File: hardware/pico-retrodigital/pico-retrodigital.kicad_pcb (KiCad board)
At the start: 2 copper layers, 50 x 38 mm, 70 parts, among them J1 Conn_02x05_Top_Bottom, J3 Conn_01x14, J4 Conn_01x02_Pin, J5 USB_C_Plug_USB2.0, U1 SN74LVC1G17DBVR, U2 SN74LVC1G17DBVR, U3 RP2354B, U4 SN74LVC245APW, U5 SN74LVC245APW, U6 SN74LVC245APW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

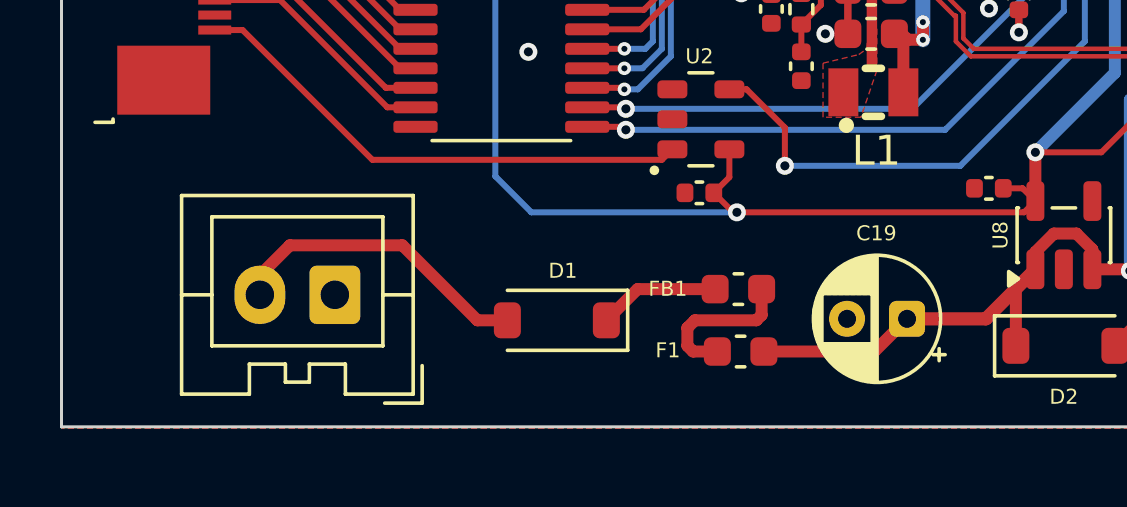
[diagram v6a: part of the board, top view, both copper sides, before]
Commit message: Add JLCPCB part numbers
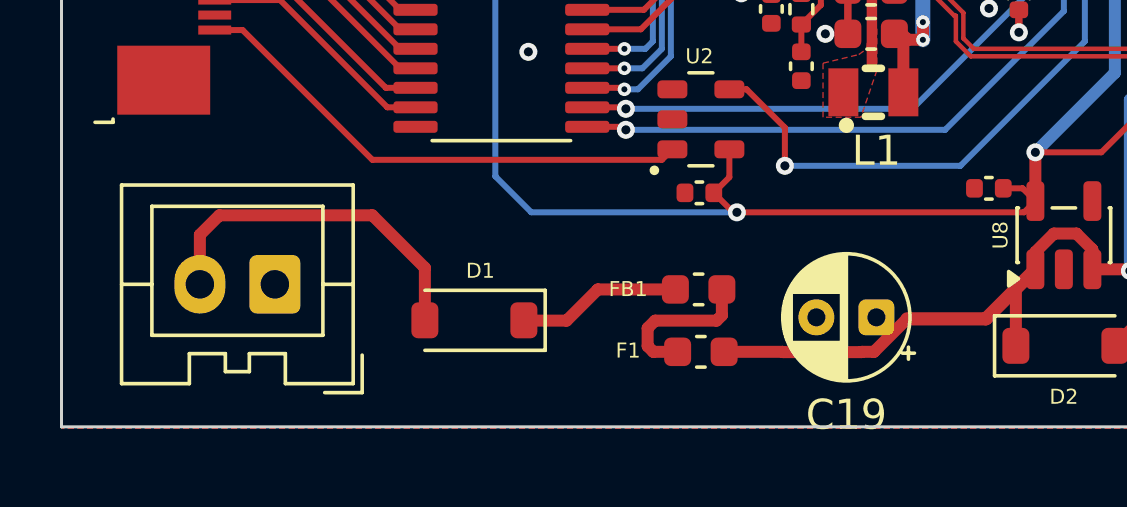
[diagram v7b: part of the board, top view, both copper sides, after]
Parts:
- moved D1 2.75 mm to (56.2, 109.9)
- moved J4 2.03 mm to (49.5, 108.7)
- moved F1 1.33 mm to (63.8, 111.0)
- moved FB1 1.33 mm to (63.7, 108.9)
- moved C19 1.02 mm to (69.6, 109.8)
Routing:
- net +5V MVS: track 10.3 -> 11.9 mm
- net Net-(D1-K): track 4.06 -> 5.48 mm
- net +5V: track 34.9 -> 36.2 mm
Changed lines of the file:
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@@
 			(net "+1V1")
 			(pinfunction "1_1")
-			(pintype "unspecified")
+			(pintype "passive")
 		)
 		(pad "2" smd rect
@@
 			(net "Net-(U3-VREG_LX)")
 			(pinfunction "2_2")
-			(pintype "unspecified")
+			(pintype "passive")
 		)
 		(embedded_fonts no)
@@
 			)
 		)
+		(property "JLCPCB" "C92589"
+			(at 0 0 0)
+			(unlocked yes)
+			(layer "F.Fab")
+			(hide yes)
+			(effects
+				(font
+					(size 0.5 0.5)
+					(thickness 0.125)
+				)
+			)
+		)
 		(sheetname "/")
 		(sheetfile "pico-retrodigital.kicad_sch")
@@
 		(sheetname "/")
 		(sheetfile "pico-retrodigital.kicad_sch")
+		(units
+			(unit
+				(name "A")
+				(pins "1" "2")
+			)
+		)
 		(attr smd)
 		(duplicate_pad_numbers_are_jumpers no)
@@
 	(footprint "Connector_JST:JST_XA_B02B-XASK-1_1x02_P2.50mm_Vertical"
 		(layer "F.Cu")
-		(at 51.55 109.05 180)
+		(at 49.55 108.7 180)
 		(descr "JST XA series connector, B02B-XASK-1 (https://www.jst.com/wp-content/uploads/2021/01/eXA1.pdf)")
 		(tags "connector JST XA vertical")
@@
 		(sheetname "/")
 		(sheetfile "pico-retrodigital.kicad_sch")
+		(units
+			(unit
+				(name "A")
+				(pins "1" "2")
+			)
+		)
 		(attr smd)
 		(duplicate_pad_numbers_are_jumpers no)
@@
 	(footprint "Capacitor_SMD:C_0603_1608Metric"
 		(layer "F.Cu")
-		(at 65.075 110.94)
+		(at 63.75 110.95)
 		(descr "Capacitor SMD 0603 (1608 Metric), square (rectangular) end terminal, IPC-7351 nominal, (Body size source: IPC-SM-782 page 76, https://www.pcb-3d.com/wordpress/wp-content/uploads/ipc-sm-782a_amendment_1_and_2.pdf)")
 		(tags "capacitor")
@@
 		(sheetname "/")
 		(sheetfile "pico-retrodigital.kicad_sch")
+		(units
+			(unit
+				(name "A")
+				(pins "1" "2")
+			)
+		)
 		(attr smd)
 		(duplicate_pad_numbers_are_jumpers no)
@@
 	(footprint "Diode_SMD:D_SOD-123"
 		(layer "F.Cu")
-		(at 58.95 109.9 180)
+		(at 56.2 109.9 180)
 		(descr "SOD-123")
 		(tags "SOD-123")
@@
 	(footprint "Capacitor_SMD:C_0603_1608Metric"
 		(layer "F.Cu")
-		(at 65 108.86)
+		(at 63.675 108.87)
 		(descr "Capacitor SMD 0603 (1608 Metric), square (rectangular) end terminal, IPC-7351 nominal, (Body size source: IPC-SM-782 page 76, https://www.pcb-3d.com/wordpress/wp-content/uploads/ipc-sm-782a_amendment_1_and_2.pdf)")
 		(tags "capacitor")
@@
 		(sheetname "/")
 		(sheetfile "pico-retrodigital.kicad_sch")
+		(units
+			(unit
+				(name "A")
+				(pins "1" "2")
+			)
+		)
 		(attr smd)
 		(duplicate_pad_numbers_are_jumpers no)
@@
 			(net "Net-(U3-VREG_AVDD)")
 			(pinfunction "VREG_AVDD_61")
-			(pintype "unspecified")
+			(pintype "passive")
 			(thermal_bridge_angle 45)
 		)
@@
 		(sheetname "/")
 		(sheetfile "pico-retrodigital.kicad_sch")
+		(units
+			(unit
+				(name "A")
+				(pins "1" "2" "3" "4" "5" "6" "7" "8" "9" "10" "11" "12" "13" "14" "15"
+					"16" "32" "31" "30" "29" "28" "27" "26" "25" "24" "23" "22" "21" "20"
+					"19" "18" "17"
+				)
+			)
+		)
 		(attr smd)
 		(duplicate_pad_numbers_are_jumpers no)
@@
 			)
 		)
+		(property "JLCPCB" "C92589"
+			(at 0 0 0)
+			(unlocked yes)
+			(layer "F.Fab")
+			(hide yes)
+			(effects
+				(font
+					(size 0.5 0.5)
+					(thickness 0.125)
+				)
+			)
+		)
 		(sheetname "/")
 		(sheetfile "pico-retrodigital.kicad_sch")
@@
 	(footprint "Capacitor_THT:CP_Radial_D4.0mm_P2.00mm"
 		(layer "F.Cu")
-		(at 70.6226 109.85 180)
+		(at 69.6 109.8 180)
 		(descr "CP, Radial series, Radial, pin pitch=2.00mm, diameter=4mm, height=7mm, Electrolytic Capacitor")
 		(tags "CP Radial series Radial pin pitch 2.00mm diameter 4mm height 7mm Electrolytic Capacitor")
 		(property "Reference" "C19"
-			(at 1.0226 2.85 0)
+			(at 1 -3.25 180)
 			(layer "F.SilkS")
 			(effects
 				(font
-					(size 0.5 0.5)
-					(thickness 0.125)
+					(size 1 1)
+					(thickness 0.15)
 				)
 			)
 		)
 		(property "Value" "47u"
-			(at 1 3.25 0)
+			(at 1 3.25 180)
 			(layer "F.Fab")
-			(hide yes)
 			(effects
 				(font
@@
 		)
 		(property "Datasheet" ""
-			(at 0 0 0)
+			(at 0 0 180)
 			(layer "F.Fab")
 			(hide yes)
@@
 				(font
 					(size 1.27 1.27)
-					(thickness 0.15)
 				)
 			)
 		)
 		(property "Description" "Polarized capacitor"
-			(at 0 0 0)
+			(at 0 0 180)
 			(layer "F.Fab")
 			(hide yes)
@@
 				(font
 					(size 1.27 1.27)
+				)
+			)
+		)
+		(property "KiLib_Generator" "capacitor/THT/other"
+			(at 0 0 180)
+			(layer "F.SilkS")
+			(hide yes)
+			(effects
+				(font
+					(size 1 1)
 					(thickness 0.15)
 				)
@@
 		)
 		(fp_text user "${REFERENCE}"
-			(at 1 0 0)
+			(at 1 0 180)
 			(layer "F.Fab")
 			(effects
@@
 		)
 		(embedded_fonts no)
-		(model "${KICAD9_3DMODEL_DIR}/Capacitor_THT.3dshapes/CP_Radial_D4.0mm_P2.00mm.step"
+		(model "${KICAD10_3DMODEL_DIR}/Capacitor_THT.3dshapes/CP_Radial_D4.0mm_P2.00mm.step"
 			(offset
 				(xyz 0 0 0)
@@
 		(sheetname "/")
 		(sheetfile "pico-retrodigital.kicad_sch")
+		(units
+			(unit
+				(name "A")
+				(pins "1" "2")
+			)
+		)
 		(attr smd)
 		(duplicate_pad_numbers_are_jumpers no)
@@
 		(sheetname "/")
 		(sheetfile "pico-retrodigital.kicad_sch")
+		(units
+			(unit
+				(name "A")
+				(pins "1" "2")
+			)
+		)
 		(attr smd)
 		(duplicate_pad_numbers_are_jumpers no)
@@
 	)
 	(segment
+		(start 69.119598 110.95)
+		(end 69.109598 110.96)
+		(width 0.4)
+		(layer "F.Cu")
+		(net "+5V")
+	)
+	(segment
+		(start 66.490402 110.96)
+		(end 66.480402 110.95)
+		(width 0.4)
+		(layer "F.Cu")
+		(net "+5V")
+	)
+	(segment
 		(start 70.6226 109.85)
-		(end 69.5326 110.94)
+		(end 69.5226 110.95)
+		(width 0.4)
+		(layer "F.Cu")
+		(net "+5V")
+	)
+	(segment
+		(start 69.109598 110.96)
+		(end 66.490402 110.96)
 		(width 0.4)
 		(layer "F.Cu")
@@
 	)
 	(segment
+		(start 69.5226 110.95)
+		(end 69.119598 110.95)
+		(width 0.4)
+		(layer "F.Cu")
+		(net "+5V")
+	)
+	(segment
 		(start 75.517499 107.007501)
 		(end 76.27 107.007501)
@@
 	)
 	(segment
-		(start 69.5326 110.94)
-		(end 65.85 110.94)
+		(start 82.25 98.35)
+		(end 82.25 99.56)
 		(width 0.4)
 		(layer "F.Cu")
@@
 	)
 	(segment
-		(start 82.25 98.35)
-		(end 82.25 99.56)
+		(start 76.8 107.537501)
+		(end 76.8 108.2)
 		(width 0.4)
 		(layer "F.Cu")
@@
 	)
 	(segment
-		(start 76.8 107.537501)
-		(end 76.8 108.2)
+		(start 66.480402 110.95)
+		(end 64.525 110.95)
 		(width 0.4)
 		(layer "F.Cu")
@@
 	)
 	(segment
-		(start 49.05 108.4)
-		(end 50.05 107.4)
+		(start 54.55 108.15)
+		(end 54.55 109.9)
 		(width 0.4)
 		(layer "F.Cu")
@@
 	)
 	(segment
-		(start 53.8 107.4)
-		(end 56.3 109.9)
+		(start 47.05 107.05)
+		(end 47.7 106.4)
 		(width 0.4)
 		(layer "F.Cu")
@@
 	)
 	(segment
-		(start 49.05 109.05)
-		(end 49.05 108.4)
+		(start 52.8 106.4)
+		(end 54.55 108.15)
 		(width 0.4)
 		(layer "F.Cu")
@@
 	)
 	(segment
-		(start 50.05 107.4)
-		(end 53.8 107.4)
+		(start 47.05 108.7)
+		(end 47.05 107.05)
 		(width 0.4)
 		(layer "F.Cu")
@@
 	)
 	(segment
-		(start 56.3 109.9)
-		(end 57.3 109.9)
+		(start 47.7 106.4)
+		(end 52.8 106.4)
 		(width 0.4)
 		(layer "F.Cu")
@@
 	)
 	(segment
-		(start 63.55 109.9)
-		(end 65.6 109.9)
+		(start 62.225 109.91)
+		(end 64.275 109.91)
 		(width 0.4)
 		(layer "F.Cu")
@@
 	)
 	(segment
-		(start 63.3 110.75)
-		(end 63.3 110.15)
+		(start 61.975 110.76)
+		(end 61.975 110.16)
 		(width 0.4)
 		(layer "F.Cu")
@@
 	)
 	(segment
-		(start 63.3 110.15)
-		(end 63.55 109.9)
+		(start 61.975 110.16)
+		(end 62.225 109.91)
 		(width 0.4)
 		(layer "F.Cu")
@@
 	)
 	(segment
-		(start 63.49 110.94)
-		(end 63.3 110.75)
+		(start 62.165 110.95)
+		(end 61.975 110.76)
 		(width 0.4)
 		(layer "F.Cu")
@@
 	)
 	(segment
-		(start 64.3 110.94)
-		(end 63.49 110.94)
+		(start 62.975 110.95)
+		(end 62.165 110.95)
 		(width 0.4)
 		(layer "F.Cu")
@@
 	)
 	(segment
-		(start 65.775 109.725)
-		(end 65.775 108.86)
+		(start 64.45 109.735)
+		(end 64.45 108.87)
 		(width 0.4)
 		(layer "F.Cu")
@@
 	)
 	(segment
-		(start 65.6 109.9)
-		(end 65.775 109.725)
+		(start 64.275 109.91)
+		(end 64.45 109.735)
 		(width 0.4)
 		(layer "F.Cu")
@@
 	)
 	(segment
-		(start 61.64 108.86)
-		(end 60.6 109.9)
+		(start 60.315 108.87)
+		(end 59.275 109.91)
+		(width 0.4)
+		(layer "F.Cu")
+		(net "Net-(D1-K)")
+	)
+	(segment
+		(start 59.275 109.91)
+		(end 57.86 109.91)
+		(width 0.4)
+		(layer "F.Cu")
+		(net "Net-(D1-K)")
+	)
+	(segment
+		(start 57.86 109.91)
+		(end 57.85 109.9)
 		(width 0.4)
 		(layer "F.Cu")
@@
 	)
 	(segment
-		(start 64.225 108.86)
-		(end 61.64 108.86)
+		(start 62.9 108.87)
+		(end 60.315 108.87)
 		(width 0.4)
 		(layer "F.Cu")
